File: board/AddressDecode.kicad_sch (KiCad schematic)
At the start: 26 parts, among them U10 74F20, U11 74F08, U12 74F86, U13 74F32, U14 74F30, U15 74F00, U16 74F32, U19 74LS154, U20 74F138, U21 74F541, U22 74F240, U8 74LS260, U9 74LS260

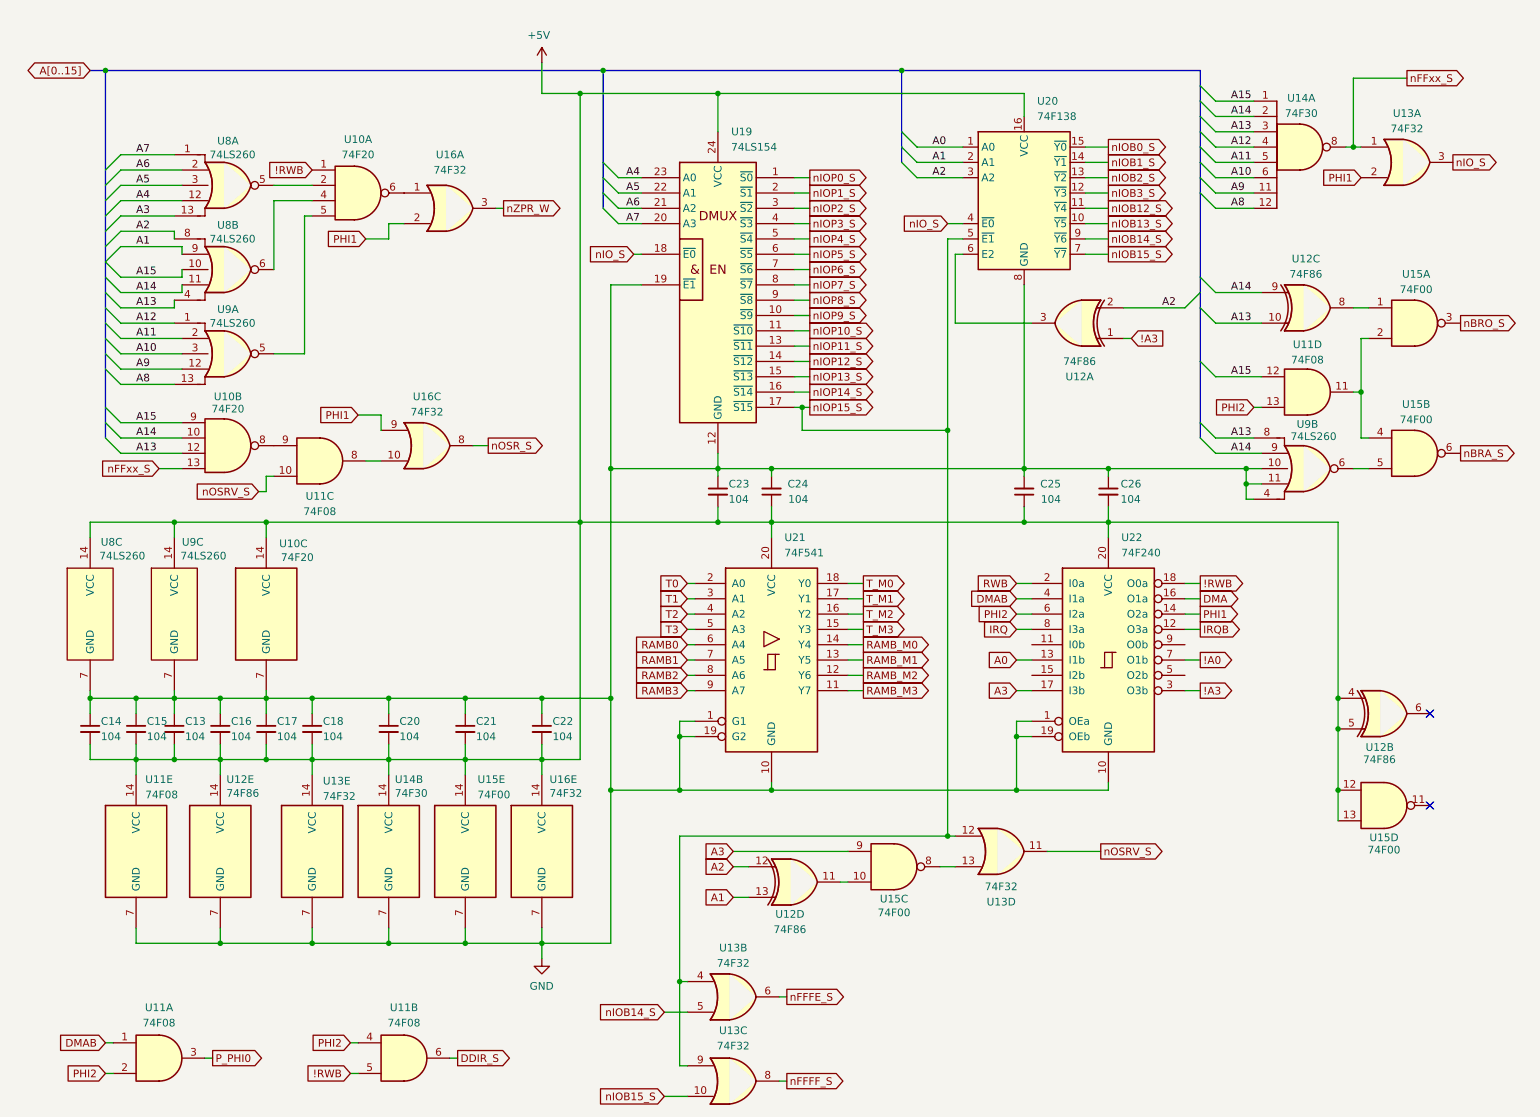
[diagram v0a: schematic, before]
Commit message: V2.0 changes with new S register and simplified logic
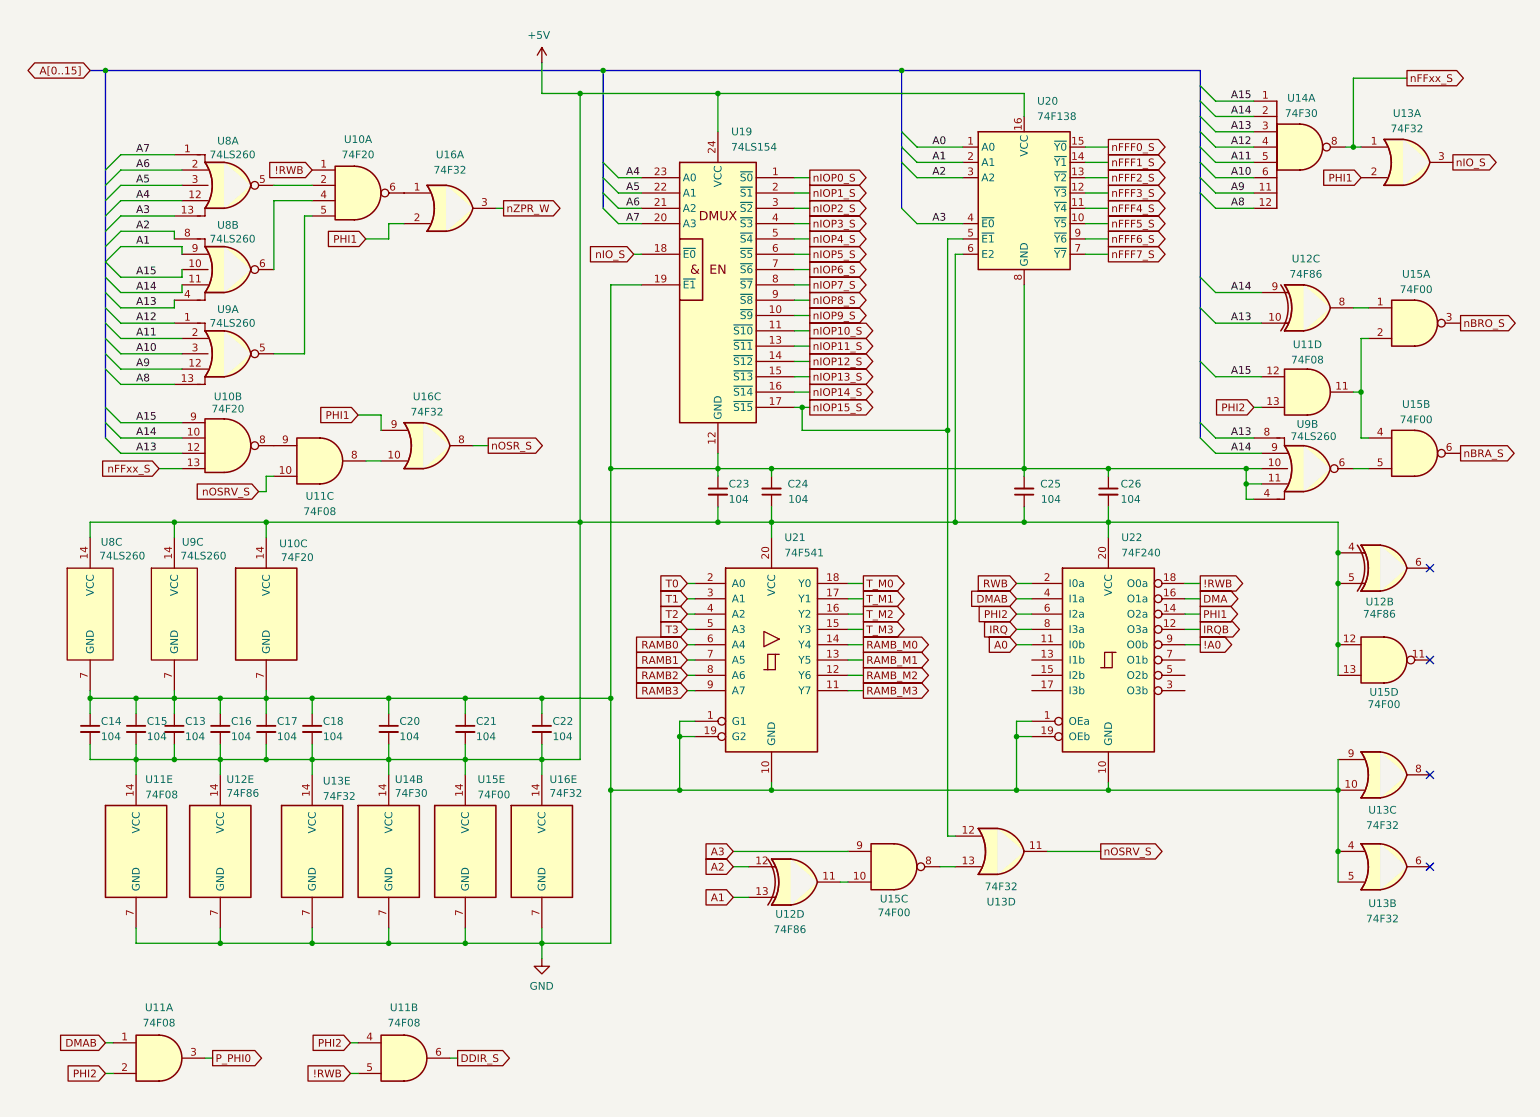
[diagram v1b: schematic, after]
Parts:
- removed unit 1 of U12
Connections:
- net !A0: now also U22.9 (O0b); no longer U22.7 (O1b)
- net +5V: now also U20.6 (E2)
- net A0: now also U22.11 (I0b); no longer U22.13 (I1b)
- net A3: now also U20.4 (~{E0}); no longer U22.17 (I3b)
- net GND: now also U13.10, U13.4, U13.5, U13.9
- net nIOP15_S: no longer U13.4, U13.9
- net nIO_S: no longer U20.4 (~{E0})
- net !A3: no longer names the net of U22.3 (O3b)
- net nFFFE_S: no longer names the net of U13.6
- net nFFFF_S: no longer names the net of U13.8
- net nIOB0_S renamed nFFF0_S
- net nIOB12_S renamed nFFF4_S
- net nIOB13_S renamed nFFF5_S
- net nIOB14_S renamed nFFF6_S
- net nFFF6_S: no longer U13.5
- net nIOB15_S renamed nFFF7_S
- net nFFF7_S: no longer U13.10
- net nIOB1_S renamed nFFF1_S
- net nIOB2_S renamed nFFF2_S
- net nIOB3_S renamed nFFF3_S
- no-connect marks 2 -> 4
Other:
- moved on the sheet: U12B, U15D

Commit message: V2.0 updates and new hydra breakout and counter cards.
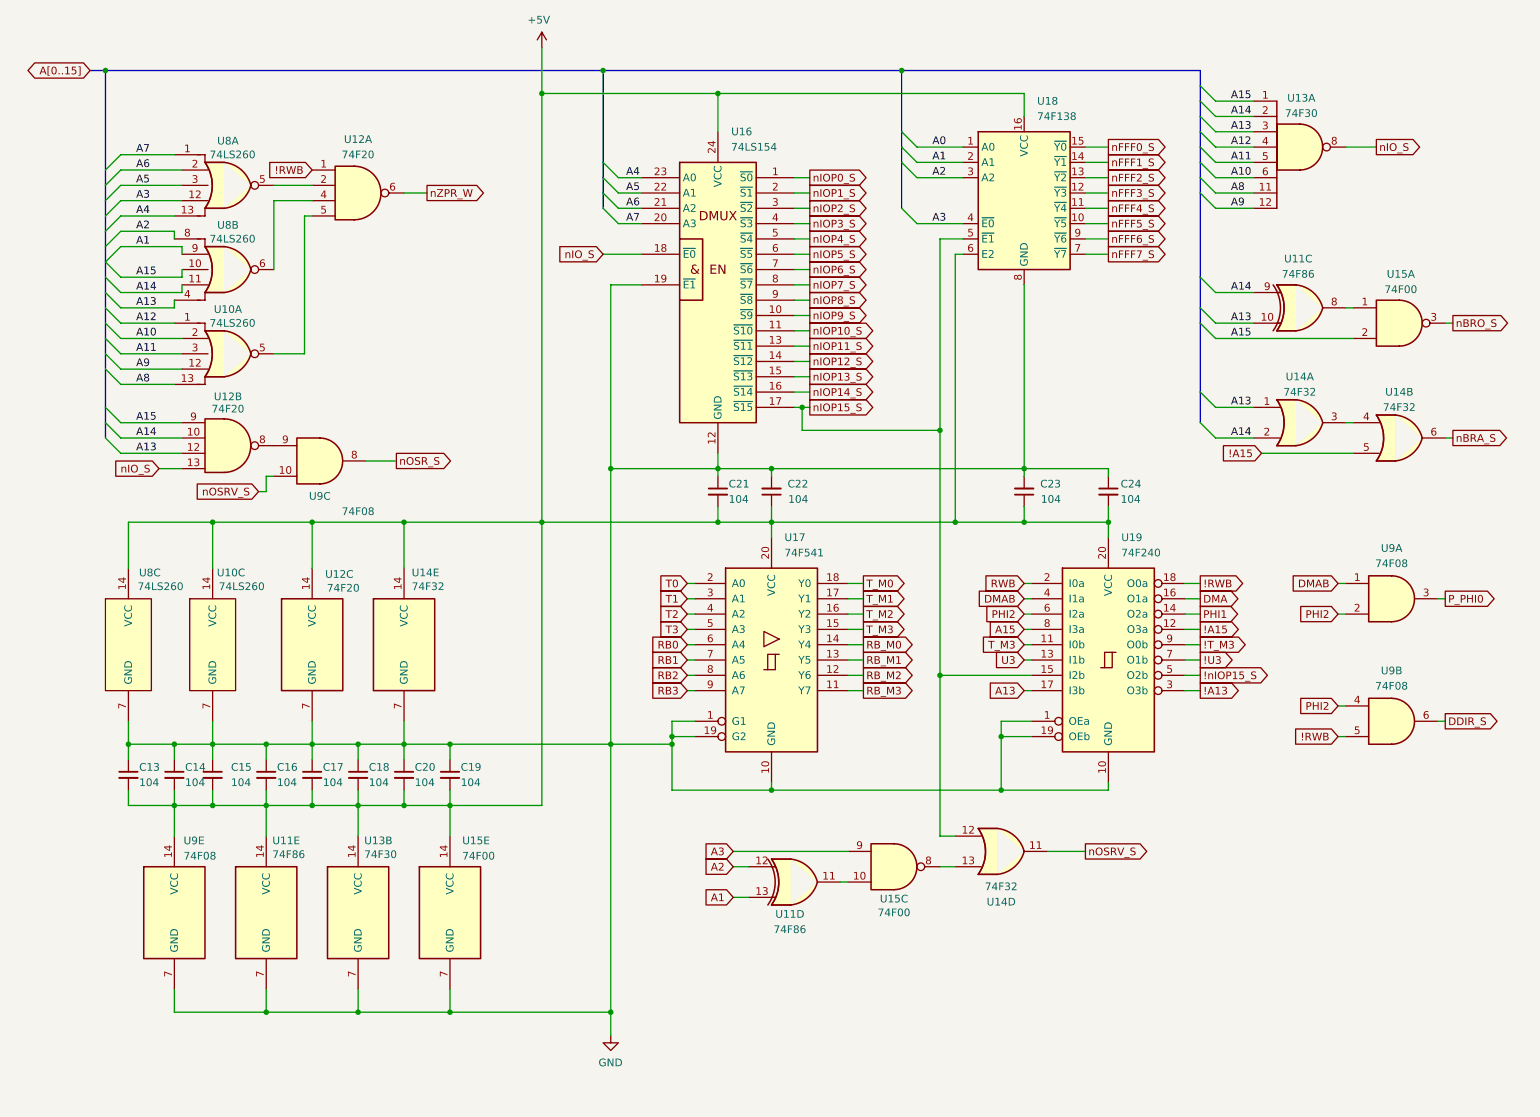
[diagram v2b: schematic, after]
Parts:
- removed C18: 104, Capacitor_THT:C_Disc_D5.0mm_W2.5mm_P5.00mm, symbol Device:C_Small
- removed unit 4 of U11
- removed unit 2 of U12
- removed unit 5 of U13
- removed unit 1 of U13
- removed unit 3 of U13
- removed unit 2 of U13
- removed unit 2 of U15
- removed unit 4 of U15
- removed U16: 74F32, Package_DIP:DIP-14_W7.62mm_Socket_LongPads, symbol 74xx:74LS32
- removed unit 2 of U9
- added unit 1 of U14
- added unit 5 of U14
- added unit 2 of U14
- renumbered C14 to C13, C15 to C14, C13 to C15, C20 to C18, C21 to C19, C22 to C20, C23 to C21, C24 to C22, C25 to C23, C26 to C24, U9 to U10, U12 to U11, U10 to U12, U14 to U13, U13 to U14, U19 to U16, U21 to U17, U20 to U18, U22 to U19, U11 to U9
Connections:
- net IRQ is gone; now on net A15: U19.8 (I3a)
- net nFFxx_S is gone; now on net nIO_S: U12.13, U13.8
- net +5V: now also U14.14 (VCC)
- net A0: no longer U19.11 (I0b)
- net A10: now also U10.2; no longer U10.3
- net A11: now also U10.3; no longer U10.2
- net A13: now also U19.17 (I3b), U14.1
- net A14: now also U14.2
- net A15: now also U15.2
- net A3: now also U8.12; no longer U8.13
- net A4: now also U8.13; no longer U8.12
- net A8: now also U13.11; no longer U13.12
- net A9: now also U13.12; no longer U13.11
- net GND: now also U14.7 (GND)
- net T_M3: now also U19.11 (I0b)
- net nBRA_S: now also U14.6
- net nIOP15_S: now also U19.15 (I2b)
- net nOSR_S: now also U9.8
- net nZPR_W: now also U12.6
- net U3: now reaches U19.13 (I1b)
- net !A13: now reaches U19.3 (O3b)
- net !nIOP15_S: now reaches U19.5 (O2b)
- net !U3: now reaches U19.7 (O1b)
- net !A0 renamed !T_M3
- net IRQB renamed !A15
- net !A15: now also U14.5
- net RAMB0 renamed RB0
- net RAMB1 renamed RB1
- net RAMB2 renamed RB2
- net RAMB3 renamed RB3
- net RAMB_M0 renamed RB_M0
- net RAMB_M1 renamed RB_M1
- net RAMB_M2 renamed RB_M2
- net RAMB_M3 renamed RB_M3
- new net: U14.3, U14.4
- no-connect marks 4 -> 0
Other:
- title: Address Decode Logic -> ZeroPage $00/$01 Mirror Memory and RAM/ROM Bank Logic
- moved on the sheet: C13, C14, C15, C16, C17, C18, C19, C20, U10C, U11C, U11E, U12C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
